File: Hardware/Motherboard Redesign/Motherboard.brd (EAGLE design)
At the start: 106.7 x 89.7 mm, 115 parts, among them J1 U.FL, J2 AVR_SPI_PRG_6PTH, U2 ATMEGA328P_PDIP, U3_MUX 74HC4052D,653, U4_MUX 74HC4052D,653, U5_MUX 74HC4052D,653, U6_MUX 74HC4052D,653, U7_MUX 74HC4052D,653, Y1 8MHz

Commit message: fixed more
I saw a problem
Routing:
- net RS485_4_TX: track 18.6 -> 17.9 mm
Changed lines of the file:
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@@
 <?xml version="1.0" encoding="utf-8"?>
 <!DOCTYPE eagle SYSTEM "eagle.dtd">
-<eagle version="7.1.0">
+<eagle version="6.5.0">
 <drawing>
 <settings>
@@
 <pass name="Default">
 <param name="RoutingGrid" value="50mil"/>
-<param name="AutoGrid" value="1"/>
-<param name="Efforts" value="0"/>
-<param name="TopRouterVariant" value="1"/>
 <param name="tpViaShape" value="round"/>
 <param name="PrefDir.1" value="|"/>
@@
 <attribute name="SUPPLIER" value="NXP" x="38.1" y="29.21" size="1.778" layer="27" rot="R270" display="off"/>
 <attribute name="OC_FARNELL" value="1826642" x="38.1" y="29.21" size="1.778" layer="27" rot="R270" display="off"/>
-<attribute name="NAME" x="43.815" y="31.3944" size="1.016" layer="25" ratio="10" rot="SR270"/>
+<attribute name="NAME" x="33.53435" y="29.21" size="1.016" layer="25" ratio="10" rot="SR0"/>
 </element>
 <element name="U4_MUX" library="4x1_Dual_Mux" package="SOIC127P600X175-16N" value="74HC4052D,653" x="59.69" y="4.445" smashed="yes" rot="R270">
@@
 <attribute name="SUPPLIER" value="NXP" x="93.98" y="4.445" size="1.778" layer="27" rot="R90" display="off"/>
 <attribute name="OC_FARNELL" value="1826642" x="93.98" y="4.445" size="1.778" layer="27" rot="R90" display="off"/>
-<attribute name="NAME" x="88.265" y="2.2606" size="1.016" layer="25" ratio="10" rot="SR90"/>
+<attribute name="NAME" x="94.81185" y="3.96875" size="1.016" layer="25" ratio="10" rot="SR0"/>
 </element>
 <element name="U6_MUX" library="4x1_Dual_Mux" package="SOIC127P600X175-16N" value="74HC4052D,653" x="59.69" y="55.88" smashed="yes" rot="R270">
@@
 <attribute name="SUPPLIER" value="NXP" x="59.69" y="55.88" size="1.778" layer="27" rot="R270" display="off"/>
 <attribute name="OC_FARNELL" value="1826642" x="59.69" y="55.88" size="1.778" layer="27" rot="R270" display="off"/>
-<attribute name="NAME" x="65.405" y="58.0644" size="1.016" layer="25" ratio="10" rot="SR270"/>
+<attribute name="NAME" x="60.83935" y="54.76875" size="1.016" layer="25" ratio="10" rot="SR0"/>
 </element>
 <element name="U7_MUX" library="4x1_Dual_Mux" package="SOIC127P600X175-16N" value="74HC4052D,653" x="95.25" y="55.88" smashed="yes" rot="R90">
@@
 <attribute name="SUPPLIER" value="NXP" x="95.25" y="55.88" size="1.778" layer="27" rot="R90" display="off"/>
 <attribute name="OC_FARNELL" value="1826642" x="95.25" y="55.88" size="1.778" layer="27" rot="R90" display="off"/>
-<attribute name="NAME" x="89.535" y="53.6956" size="1.016" layer="25" ratio="10" rot="SR90"/>
+<attribute name="NAME" x="96.71685" y="54.9275" size="1.016" layer="25" ratio="10" rot="SR0"/>
 </element>
 <element name="Y1" library="SparkFun-FreqCtrl" package="HC49US" value="8MHz" x="3.81" y="34.29" rot="R90"/>
@@
 <contactref element="U6_MUX" pad="3"/>
 <via x="52.705" y="64.77" extent="1-16" drill="0.3302" shape="square"/>
-<wire x1="52.705" y1="64.77" x2="52.705" y2="72.39" width="0.1524" layer="16"/>
-<wire x1="52.705" y1="72.39" x2="51.435" y2="73.66" width="0.1524" layer="16"/>
-<wire x1="51.435" y1="73.66" x2="48.26" y2="73.66" width="0.1524" layer="16"/>
+<wire x1="52.705" y1="64.77" x2="52.705" y2="73.025" width="0.1524" layer="16"/>
+<wire x1="52.07" y1="73.66" x2="48.26" y2="73.66" width="0.1524" layer="16"/>
 <wire x1="52.705" y1="64.77" x2="57.62625" y2="59.84875" width="0.1524" layer="1"/>
 <wire x1="57.62625" y1="59.84875" x2="60.80125" y2="59.84875" width="0.1524" layer="1"/>
 <wire x1="60.80125" y1="59.84875" x2="61.595" y2="59.055" width="0.1524" layer="1"/>
 <wire x1="61.595" y1="59.055" x2="61.595" y2="58.4708" width="0.1524" layer="1"/>
+<wire x1="52.705" y1="73.025" x2="52.07" y2="73.66" width="0.1524" layer="16"/>
 </signal>
 <signal name="U7_MUX_S0">
@@
 <via x="48.26" y="62.865" extent="1-16" drill="0.3302" shape="square"/>
 <wire x1="72.52" y1="48.26" x2="72.52" y2="50.67" width="0.4064" layer="1"/>
-<wire x1="72.52" y1="50.67" x2="72.39" y2="50.8" width="0.1524" layer="1"/>
+<wire x1="72.52" y1="50.67" x2="72.39" y2="50.8" width="0.4064" layer="1"/>
 <via x="72.39" y="50.8" extent="1-16" drill="0.3302" shape="square"/>
 <wire x1="72.39" y1="50.8" x2="67.31" y2="50.8" width="0.4064" layer="16"/>
@@
 <via x="52.22875" y="16.35125" extent="1-16" drill="0.3302" diameter="0.254" shape="square"/>
 <wire x1="52.22875" y1="16.35125" x2="43.02125" y2="16.35125" width="0.1524" layer="16"/>
-<wire x1="42.545" y1="16.8275" x2="42.545" y2="28.73375" width="0.1524" layer="16"/>
-<via x="42.545" y="28.73375" extent="1-16" drill="0.3302" shape="square"/>
-<wire x1="42.545" y1="28.73375" x2="42.545" y2="31.8008" width="0.1524" layer="1"/>
+<wire x1="42.545" y1="16.8275" x2="42.545" y2="28.09875" width="0.1524" layer="16"/>
+<via x="42.545" y="28.09875" extent="1-16" drill="0.3302" shape="square"/>
+<wire x1="42.545" y1="28.09875" x2="42.545" y2="31.8008" width="0.1524" layer="1"/>
 <wire x1="43.02125" y1="16.35125" x2="42.545" y2="16.8275" width="0.1524" layer="16"/>
 </signal>
@@
 <contactref element="U4_MUX" pad="5"/>
 <wire x1="71.755" y1="12.3825" x2="71.4375" y2="12.065" width="0.1524" layer="1"/>
-<wire x1="71.4375" y1="12.065" x2="71.4375" y2="6.985" width="0.1524" layer="1"/>
-<via x="71.4375" y="6.985" extent="1-16" drill="0.3302" diameter="0.254" shape="square"/>
-<wire x1="71.4375" y1="6.985" x2="59.53125" y2="6.985" width="0.1524" layer="16"/>
+<wire x1="71.4375" y1="12.065" x2="71.4375" y2="8.255" width="0.1524" layer="1"/>
+<via x="71.4375" y="8.255" extent="1-16" drill="0.3302" diameter="0.254" shape="square"/>
 <wire x1="59.53125" y1="6.985" x2="59.055" y2="6.50875" width="0.1524" layer="16"/>
 <via x="59.055" y="6.50875" extent="1-16" drill="0.3302" diameter="0.254" shape="square"/>
 <wire x1="59.055" y1="6.50875" x2="59.055" y2="7.0358" width="0.1524" layer="1"/>
+<wire x1="59.53125" y1="6.985" x2="70.1675" y2="6.985" width="0.1524" layer="16"/>
+<wire x1="70.1675" y1="6.985" x2="71.4375" y2="8.255" width="0.1524" layer="16"/>
 </signal>
 <signal name="RS485_5_RX">
 <contactref element="RS_TRANS_9" pad="RO"/>
 <contactref element="U4_MUX" pad="15"/>
-<wire x1="70.96125" y1="6.35" x2="67.6275" y2="3.01625" width="0.1524" layer="1"/>
+<wire x1="73.50125" y1="8.89" x2="67.6275" y2="3.01625" width="0.1524" layer="1"/>
 <wire x1="67.6275" y1="3.01625" x2="63.5" y2="3.01625" width="0.1524" layer="1"/>
 <wire x1="63.5" y1="3.01625" x2="62.865" y2="2.38125" width="0.1524" layer="1"/>
 <wire x1="62.865" y1="2.38125" x2="62.865" y2="1.8542" width="0.1524" layer="1"/>
-<wire x1="70.96125" y1="6.35" x2="72.39" y2="6.35" width="0.1524" layer="1"/>
-<wire x1="72.39" y1="6.35" x2="73.81875" y2="7.77875" width="0.1524" layer="1"/>
 <wire x1="76.2" y1="12.3825" x2="76.2" y2="11.58875" width="0.1524" layer="1"/>
 <wire x1="76.2" y1="11.58875" x2="76.5175" y2="11.27125" width="0.1524" layer="1"/>
 <wire x1="76.5175" y1="11.27125" x2="76.5175" y2="9.2075" width="0.1524" layer="1"/>
 <wire x1="76.5175" y1="9.2075" x2="76.2" y2="8.89" width="0.1524" layer="1"/>
-<wire x1="76.2" y1="8.89" x2="74.13625" y2="8.89" width="0.1524" layer="1"/>
-<wire x1="74.13625" y1="8.89" x2="73.81875" y2="8.5725" width="0.1524" layer="1"/>
-<wire x1="73.81875" y1="8.5725" x2="73.81875" y2="7.77875" width="0.1524" layer="1"/>
+<wire x1="76.2" y1="8.89" x2="73.50125" y2="8.89" width="0.1524" layer="1"/>
 </signal>
 <signal name="RS485_5_TX">

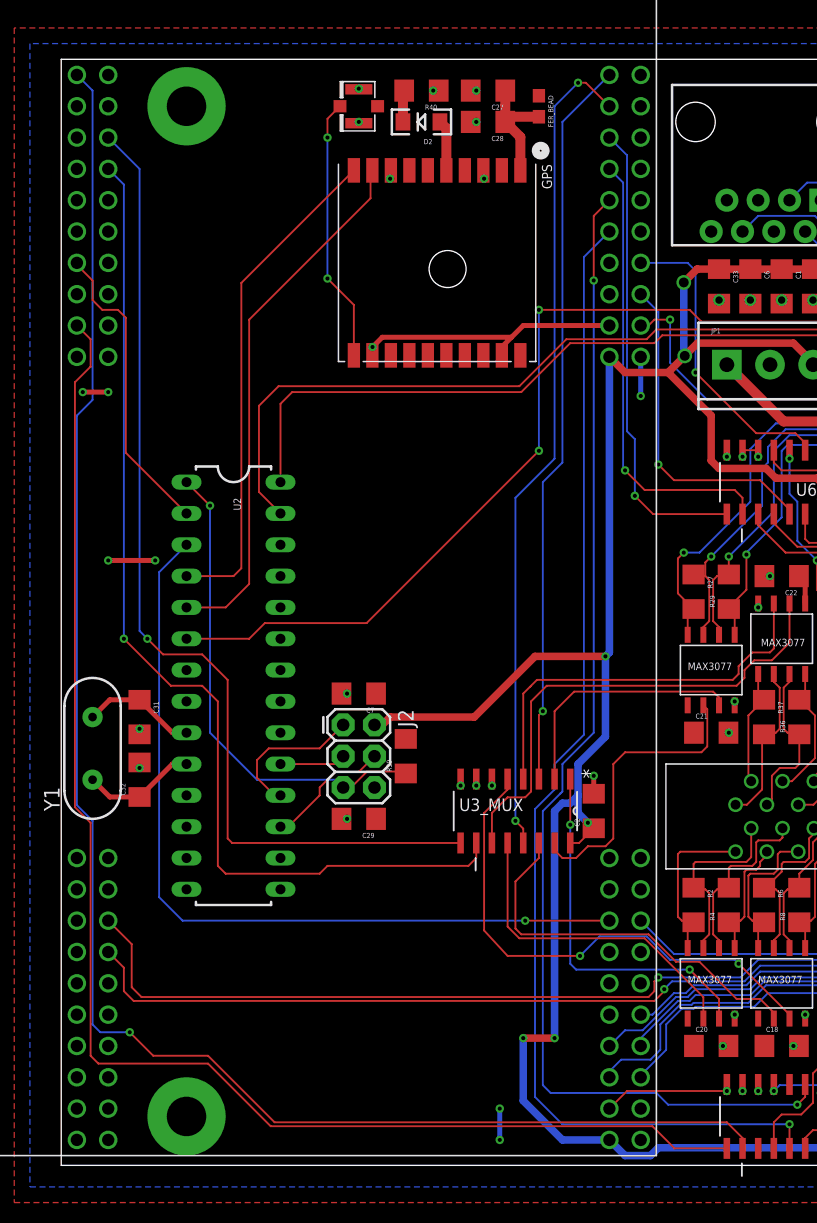
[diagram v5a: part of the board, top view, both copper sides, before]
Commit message: made wires shorter
got rid of 10+ vias and changed from square to circle vias
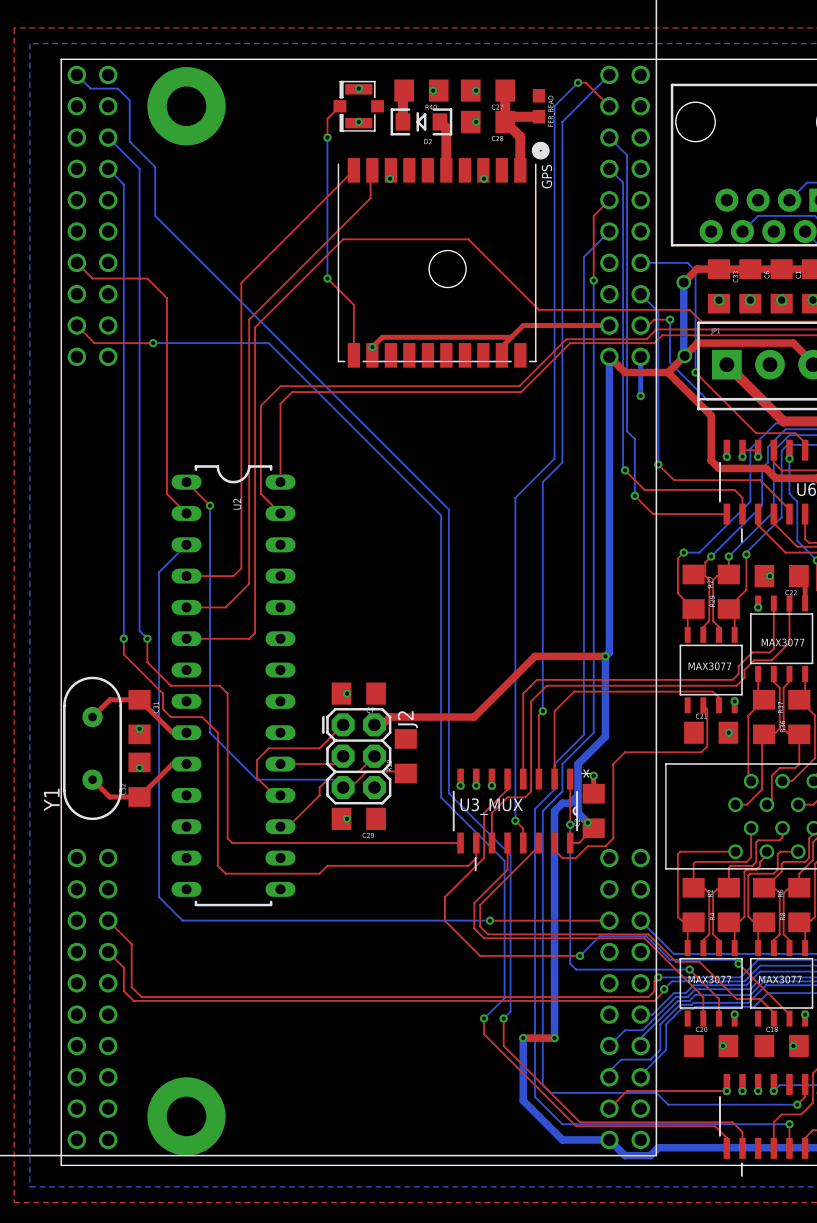
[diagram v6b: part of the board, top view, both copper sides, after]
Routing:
- net U4_MUX_S0: track 135.9 -> 118.4 mm
- net DTR: track 86.0 -> 98.5 mm, vias 2 -> 0
- net U4_MUX_S1: track 115.4 -> 104.8 mm, vias 0 -> 2
- net GND: track 72.4 -> 66.5 mm, vias 81 -> 77
- net RS485_2_TX: track 42.3 -> 46.3 mm
- net RS485_2_RX: track 32.0 -> 35.9 mm
- net RS485_1_RX: track 26.8 -> 30.7 mm
- net +3V3: track 39.9 -> 37.3 mm, vias 8 -> 6
- net U2TX: track 24.7 -> 26.6 mm

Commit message: clean up
have more questions now
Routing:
- net +3V3: track 37.3 -> 34.2 mm, vias 6 -> 5
- net +5V: track 270.9 -> 273.7 mm, vias 14 -> 13
- net U5_MUX_S1: track 106.8 -> 104.8 mm
- net U5_MUX_S0: track 103.9 -> 102.8 mm
- net 15_RX-: track 14.5 -> 13.5 mm
- net 4_RX-: track 13.3 -> 12.3 mm
- net 7_TX+: track 10.7 -> 9.88 mm
- net 17_RX-: track 13.6 -> 12.9 mm
- net 2_TX-: track 13.7 -> 13.0 mm
- net 6_RX+: track 10.3 -> 9.64 mm
- net 5_RX-: track 12.5 -> 11.8 mm
- net 8_TX+: track 11.0 -> 10.5 mm
- net RESET: vias 1 -> 0

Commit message: rg
sdgg
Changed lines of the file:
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@@
 <wire x1="43.02125" y1="3.65125" x2="36.03625" y2="10.63625" width="0.1524" layer="1"/>
 <via x="36.03625" y="12.3825" extent="1-16" drill="0.3302"/>
-<wire x1="36.03625" y1="10.63625" x2="35.56" y2="11.1125" width="0" layer="19" extent="1-16"/>
 <wire x1="37.226875" y1="25.161875" x2="32.0675" y2="30.32125" width="0.1524" layer="16"/>
 <wire x1="32.0675" y1="30.32125" x2="32.0675" y2="53.18125" width="0.1524" layer="16"/>
@@
 <wire x1="96.67875" y1="7.77875" x2="96.67875" y2="13.0175" width="0.1524" layer="1"/>
 <wire x1="96.67875" y1="13.0175" x2="94.9325" y2="14.76375" width="0.1524" layer="1"/>
-<wire x1="49.37125" y1="13.81125" x2="9.04875" y2="13.81125" width="0.1524" layer="1"/>
-<wire x1="9.04875" y1="13.81125" x2="7.14375" y2="13.81125" width="0" layer="19" extent="1-16"/>
 <wire x1="78.105" y1="14.76375" x2="94.9325" y2="14.76375" width="0.1524" layer="1"/>
 <wire x1="49.37125" y1="13.81125" x2="50.165" y2="14.605" width="0.1524" layer="1"/>
@@
 <wire x1="77.1525" y1="16.66875" x2="77.7875" y2="16.03375" width="0.1524" layer="16"/>
 <wire x1="77.7875" y1="16.03375" x2="77.7875" y2="15.39875" width="0.1524" layer="16"/>
-<wire x1="5.08" y1="17.78" x2="9.04875" y2="13.81125" width="0.1524" layer="1"/>
+<wire x1="49.37125" y1="13.81125" x2="36.35375" y2="13.81125" width="0.1524" layer="1"/>
+<wire x1="36.35375" y1="13.81125" x2="32.385" y2="17.78" width="0.1524" layer="1"/>
+<wire x1="32.385" y1="17.78" x2="5.08" y2="17.78" width="0.1524" layer="1"/>
 </signal>
 <signal name="U5_MUX_S1">
@@
 <via x="79.0575" y="15.39875" extent="1-16" drill="0.3302" diameter="0.254"/>
 <wire x1="79.0575" y1="15.39875" x2="78.89875" y2="15.5575" width="0.1524" layer="16"/>
-<wire x1="7.77875" y1="14.12875" x2="11.27125" y2="14.12875" width="0" layer="19" extent="1-16"/>
-<wire x1="11.27125" y1="14.12875" x2="48.895" y2="14.12875" width="0.1524" layer="1"/>
 <wire x1="48.895" y1="14.12875" x2="49.37125" y2="14.605" width="0.1524" layer="1"/>
 <wire x1="49.37125" y1="14.605" x2="49.37125" y2="15.39875" width="0.1524" layer="1"/>
@@
 <wire x1="57.785" y1="17.145" x2="77.31125" y2="17.145" width="0.1524" layer="16"/>
 <wire x1="77.31125" y1="17.145" x2="79.0575" y2="15.39875" width="0.1524" layer="16"/>
-<wire x1="5.08" y1="20.32" x2="11.27125" y2="14.12875" width="0.1524" layer="1"/>
+<wire x1="5.08" y1="20.32" x2="30.48" y2="20.32" width="0.1524" layer="1"/>
+<wire x1="30.48" y1="20.32" x2="36.67125" y2="14.12875" width="0.1524" layer="1"/>
+<wire x1="36.67125" y1="14.12875" x2="48.895" y2="14.12875" width="0.1524" layer="1"/>
 </signal>
 <signal name="U5TX">
@@
 <wire x1="73.81875" y1="16.98625" x2="102.07625" y2="16.98625" width="0.1524" layer="1"/>
 <wire x1="102.07625" y1="16.98625" x2="102.87" y2="17.78" width="0.1524" layer="1"/>
-<wire x1="102.87" y1="17.78" x2="103.34625" y2="18.25625" width="0" layer="19" extent="1-16"/>
 <wire x1="58.57875" y1="14.44625" x2="71.59625" y2="14.44625" width="0.1524" layer="16"/>
 <via x="71.59625" y="14.44625" extent="1-16" drill="0.3302"/>
@@
 <wire x1="80.645" y1="18.0975" x2="80.645" y2="19.71375" width="0.1524" layer="1"/>
 <wire x1="80.645" y1="19.71375" x2="81.12125" y2="20.19" width="0.1524" layer="1"/>
-<wire x1="79.85125" y1="25.55875" x2="79.85125" y2="24.41375" width="0" layer="19" extent="1-16"/>
 <wire x1="79.85125" y1="24.41375" x2="79.85125" y2="20.6375" width="0.1524" layer="1"/>
 <wire x1="79.85125" y1="20.6375" x2="80.16875" y2="20.32" width="0.1524" layer="1"/>
@@
 <wire x1="83.84875" y1="22.86" x2="83.97875" y2="22.99" width="0.1524" layer="1"/>
 <wire x1="83.97875" y1="22.99" x2="83.97875" y2="24.4475" width="0.1524" layer="1"/>
-<wire x1="83.97875" y1="24.4475" x2="83.97875" y2="24.765" width="0" layer="19" extent="1-16"/>
 <wire x1="83.02625" y1="25.4" x2="83.02625" y2="26.9875" width="0.1524" layer="1"/>
 <wire x1="85.16" y1="27.8175" x2="83.85625" y2="27.8175" width="0.1524" layer="1"/>
